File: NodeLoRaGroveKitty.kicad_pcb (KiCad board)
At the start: 2 copper layers, 50 x 50 mm, 42 parts, among them IC1 CP2104, P1 PICKIT PROGRAMMER, P2 Battery, P3 USB_B, P4 A0, P5 D9, P6 I2C, Q1 MMBT2222A, Q2 MMBT2222A, SW1 SW_RESET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

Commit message: PCB 1.0v
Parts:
- removed P1: PICKIT PROGRAMMER, Pin_Headers:Pin_Header_Straight_1x05_Pitch2.54mm
- added G***: LOGO, modules:electronic_cats_logo_4x3, F.Cu at (145.1, 105.9)
- P2: footprint Pin_Headers:Pin_Header_Angled_1x02_Pitch2.54mm -> modules:panelmate_smd_2
- moved C6 51.0 mm to (164.9, 95.4), turned to 270 degrees
- moved R6 50.9 mm to (165.4, 110.0), turned to 0 degrees
- moved Q2 48.8 mm to (164.8, 106.9), turned to 270 degrees
- moved R7 43.8 mm to (160.1, 110.1), turned to 180 degrees
- moved Q1 43.6 mm to (161.0, 106.9), turned to 270 degrees
- moved R10 41.4 mm to (162.4, 95.3), turned to 270 degrees
- moved P2 39.8 mm to (141.9, 124.0), turned to 90 degrees
- moved R14 38.4 mm to (131.2, 96.0)
- moved U1 38.4 mm to (152.4, 125.8)
- moved A1 38.4 mm to (121.7, 87.8)
- moved D1 38.4 mm to (164.7, 128.5)
- moved D2 38.4 mm to (162.0, 128.5)
- moved P4 38.4 mm to (145.2, 127.3)
- moved R13 38.4 mm to (167.2, 95.4)
- moved R15 38.4 mm to (131.2, 98.4)
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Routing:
- net +3V3: track 24.2 -> 226.9 mm, vias 0 -> 10
- net VCC: track 2.89 -> 91.3 mm, vias 0 -> 4
- net GND: track 27.8 -> 102.4 mm, vias 0 -> 14
- net /GPIO13: track 0.00 -> 66.5 mm, vias 0 -> 4
- net /SCL: track 0.00 -> 57.0 mm, vias 0 -> 2
- net /SDA: track 0.00 -> 55.1 mm, vias 0 -> 2
- net /RESET: track 0.00 -> 54.2 mm, vias 0 -> 2
- net /GPIO2: track 35.9 -> 89.2 mm, vias 0 -> 2
- net /A0: track 0.00 -> 52.2 mm, vias 0 -> 2
- net Net-(D4-Pad2): track 0.07 -> 37.9 mm, vias 0 -> 3
- net Net-(D5-Pad1): track 0.00 -> 31.6 mm, vias 0 -> 2
- net Net-(D3-Pad1): track 0.00 -> 29.3 mm, vias 0 -> 1
- net /GPIO0: track 0.00 -> 25.3 mm
- net /SRX: track 0.00 -> 21.3 mm, vias 0 -> 1
- net /STX: track 0.00 -> 20.3 mm, vias 0 -> 1
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- added copper zone on B.Cu, net GND
- added copper zone on F.Cu, net GND
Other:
- board text added: "VCC"
- board text removed: "Vcc"

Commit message: Update Labels
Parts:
- renumbered SW1 to RST
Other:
- board text added: "D13"
- board text added: "D2"
- board text removed: "02"
- board text removed: "13"
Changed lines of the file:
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@@
 (kicad_pcb (version 4) (host pcbnew 4.0.5)
   (general
-    (links 0)
-    (no_connects 1)
+    (links 105)
+    (no_connects 0)
     (area 120.109999 82.589999 170.210001 132.690001)
     (thickness 1.6)
@@
     (tags "LED led 0805 SMD smd SMT smt smdled SMDLED smtled SMTLED")
     (attr smd)
-    (fp_text reference D3 (at 2.8 0 180) (layer F.SilkS)
-      (effects (font (size 1 1) (thickness 0.15)))
-    )
-    (fp_text value CHG (at 5.05 0.05 90) (layer F.SilkS)
+    (fp_text reference D3 (at 2.8 0 180) (layer F.Fab)
+      (effects (font (size 1 1) (thickness 0.15)))
+    )
+    (fp_text value CHG (at 3.64 0.04 90) (layer F.SilkS)
       (effects (font (size 1 1) (thickness 0.15)))
     )
@@
     (tags "LED led 0805 SMD smd SMT smt smdled SMDLED smtled SMTLED")
     (attr smd)
-    (fp_text reference D4 (at -2.7 0.1 360) (layer F.SilkS)
-      (effects (font (size 1 1) (thickness 0.15)))
-    )
-    (fp_text value DONE (at -5.5 -0.05 270) (layer F.SilkS)
+    (fp_text reference D4 (at -2.7 0.1 360) (layer F.Fab)
+      (effects (font (size 1 1) (thickness 0.15)))
+    )
+    (fp_text value DONE (at -4.04 -0.04 270) (layer F.SilkS)
       (effects (font (size 1 1) (thickness 0.15)))
     )
@@
       (effects (font (size 1 1) (thickness 0.15)))
     )
-    (fp_text value Led (at -4.8 0 270) (layer F.SilkS)
+    (fp_text value Led (at -4.8 0 270) (layer F.Fab)
       (effects (font (size 1 1) (thickness 0.15)))
     )
@@
     (tags "Tactile Switch")
     (attr smd)
-    (fp_text reference SW1 (at 0.033329 2.25 90) (layer F.SilkS)
+    (fp_text reference RST (at 0.033329 2.25 90) (layer F.SilkS)
       (effects (font (size 1 1) (thickness 0.15)))
     )
@@
       (xy 1.463092 -2.5146) (xy 1.492024 -2.514153)) (layer F.SilkS) (width 0.01))
   )
-  (gr_text 13 (at 164.41 120.89 90) (layer F.SilkS)
+  (gr_text D13 (at 164.41 120.89 90) (layer F.SilkS)
     (effects (font (size 1.5 1.5) (thickness 0.2)) (justify mirror))
   )
-  (gr_text "02\n" (at 162.41 120.64 90) (layer F.SilkS)
+  (gr_text "D2\n" (at 162.41 120.64 90) (layer F.SilkS)
     (effects (font (size 1.5 1.5) (thickness 0.2)) (justify mirror))
   )

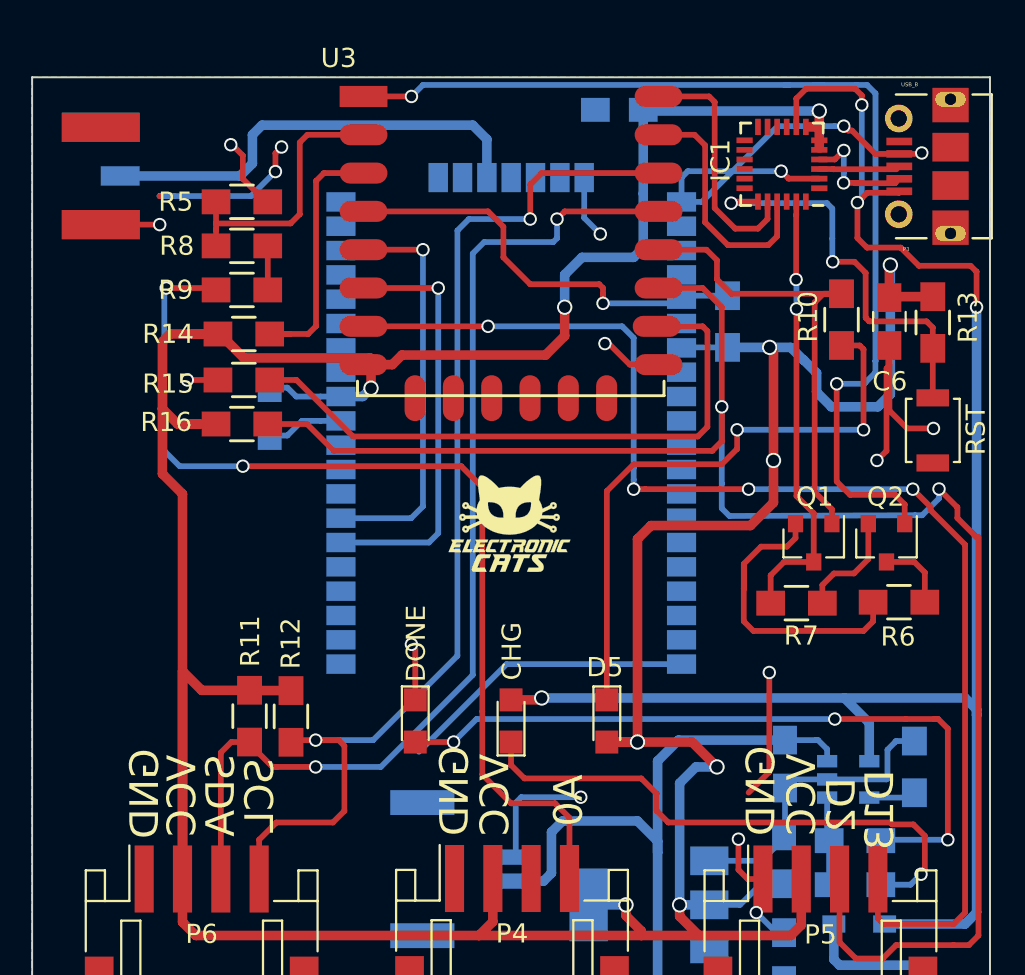
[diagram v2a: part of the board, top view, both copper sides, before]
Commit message: Update inverter label
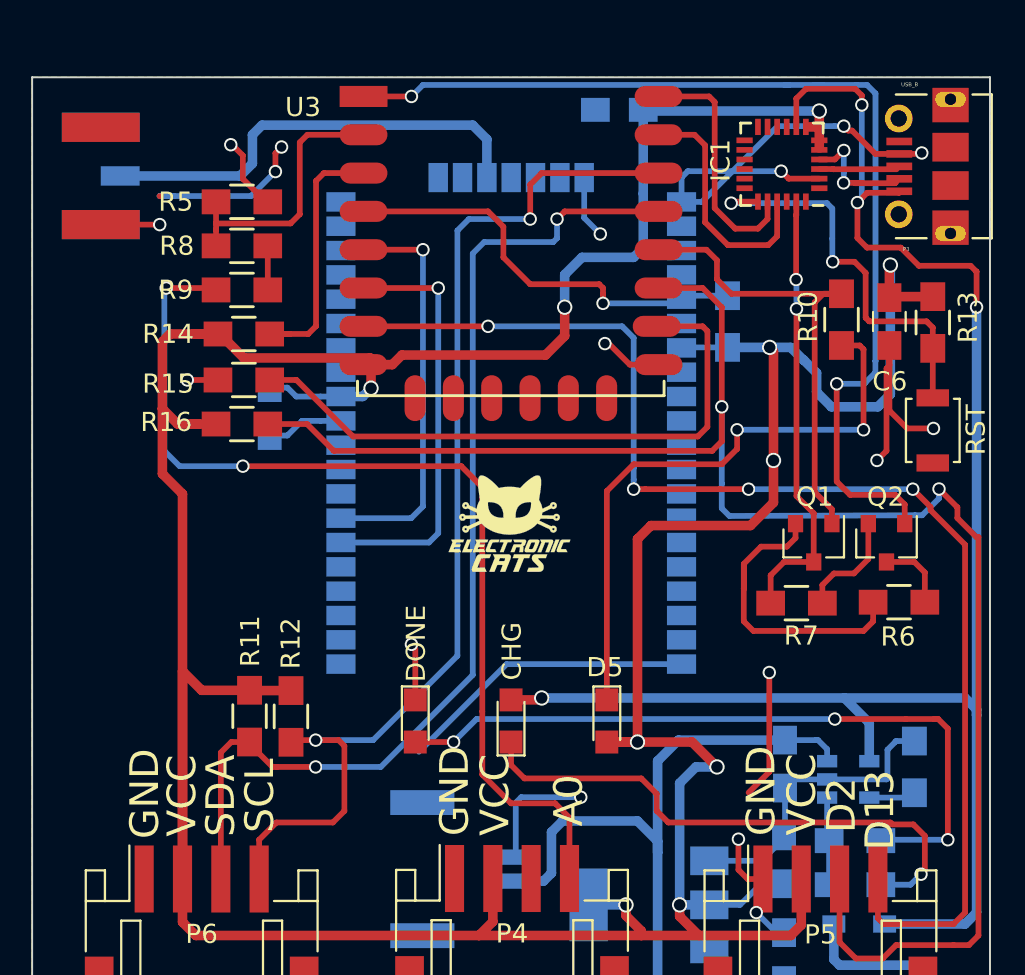
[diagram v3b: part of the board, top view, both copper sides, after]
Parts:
- renumbered MODULE1 to RN2xx3
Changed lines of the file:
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@@
     (descr "Module, ESP-8266, ESP-12, 16 pad, SMD")
     (tags "Module ESP-8266 ESP8266")
-    (fp_text reference U3 (at -2 -2) (layer F.SilkS)
+    (fp_text reference U3 (at -3.86 0.56) (layer F.SilkS)
       (effects (font (size 1 1) (thickness 0.15)))
     )
@@
   (module Library:RN2483 (layer B.Cu)
     (at 154.05858 114.544404 180)
-    (fp_text reference MODULE1 (at 2.8956 1.4478 180) (layer B.SilkS)
+    (fp_text reference RN2xx3 (at 2.95858 -1.255596 180) (layer B.SilkS)
       (effects (font (size 1 1) (thickness 0.15)) (justify mirror))
     )
@@
   )
   (gr_text D13 (at 164.41 120.89 90) (layer F.SilkS)
-    (effects (font (size 1.5 1.5) (thickness 0.2)) (justify mirror))
+    (effects (font (size 1.5 1.5) (thickness 0.2)))
   )
   (gr_text "D2\n" (at 162.41 120.64 90) (layer F.SilkS)
-    (effects (font (size 1.5 1.5) (thickness 0.2)) (justify mirror))
+    (effects (font (size 1.5 1.5) (thickness 0.2)))
   )
   (gr_text A0 (at 148.16 120.39 90) (layer F.SilkS)
-    (effects (font (size 1.5 1.5) (thickness 0.2)) (justify mirror))
+    (effects (font (size 1.5 1.5) (thickness 0.2)))
   )
   (gr_text "SCL\n" (at 132.04 120.14 90) (layer F.SilkS)
-    (effects (font (size 1.5 1.5) (thickness 0.2)) (justify mirror))
+    (effects (font (size 1.5 1.5) (thickness 0.2)))
   )
   (gr_text "SDA\n" (at 130 120.14 90) (layer F.SilkS)
-    (effects (font (size 1.5 1.5) (thickness 0.2)) (justify mirror))
+    (effects (font (size 1.5 1.5) (thickness 0.2)))
   )
   (gr_text VCC (at 127.98 120.14 90) (layer F.SilkS)
-    (effects (font (size 1.5 1.5) (thickness 0.2)) (justify mirror))
+    (effects (font (size 1.5 1.5) (thickness 0.2)))
   )
   (gr_text VCC (at 144.32 120.1 90) (layer F.SilkS)
-    (effects (font (size 1.5 1.5) (thickness 0.2)) (justify mirror))
+    (effects (font (size 1.5 1.5) (thickness 0.2)))
   )
   (gr_text "VCC\n\n" (at 161.54 120.08 90) (layer F.SilkS)
-    (effects (font (size 1.5 1.5) (thickness 0.2)) (justify mirror))
+    (effects (font (size 1.5 1.5) (thickness 0.2)))
   )
   (gr_text GND (at 158.21 119.89 90) (layer F.SilkS)
-    (effects (font (size 1.5 1.5) (thickness 0.2)) (justify mirror))
+    (effects (font (size 1.5 1.5) (thickness 0.2)))
   )
   (gr_text GND (at 142.21 119.89 90) (layer F.SilkS)
-    (effects (font (size 1.5 1.5) (thickness 0.2)) (justify mirror))
+    (effects (font (size 1.5 1.5) (thickness 0.2)))
   )
   (gr_text GND (at 126.035 120.04 90) (layer F.SilkS)
-    (effects (font (size 1.5 1.5) (thickness 0.2)) (justify mirror))
+    (effects (font (size 1.5 1.5) (thickness 0.2)))
   )
   (gr_line (start 170.16 82.64) (end 170.16 132.64) (layer Edge.Cuts) (width 0.1))

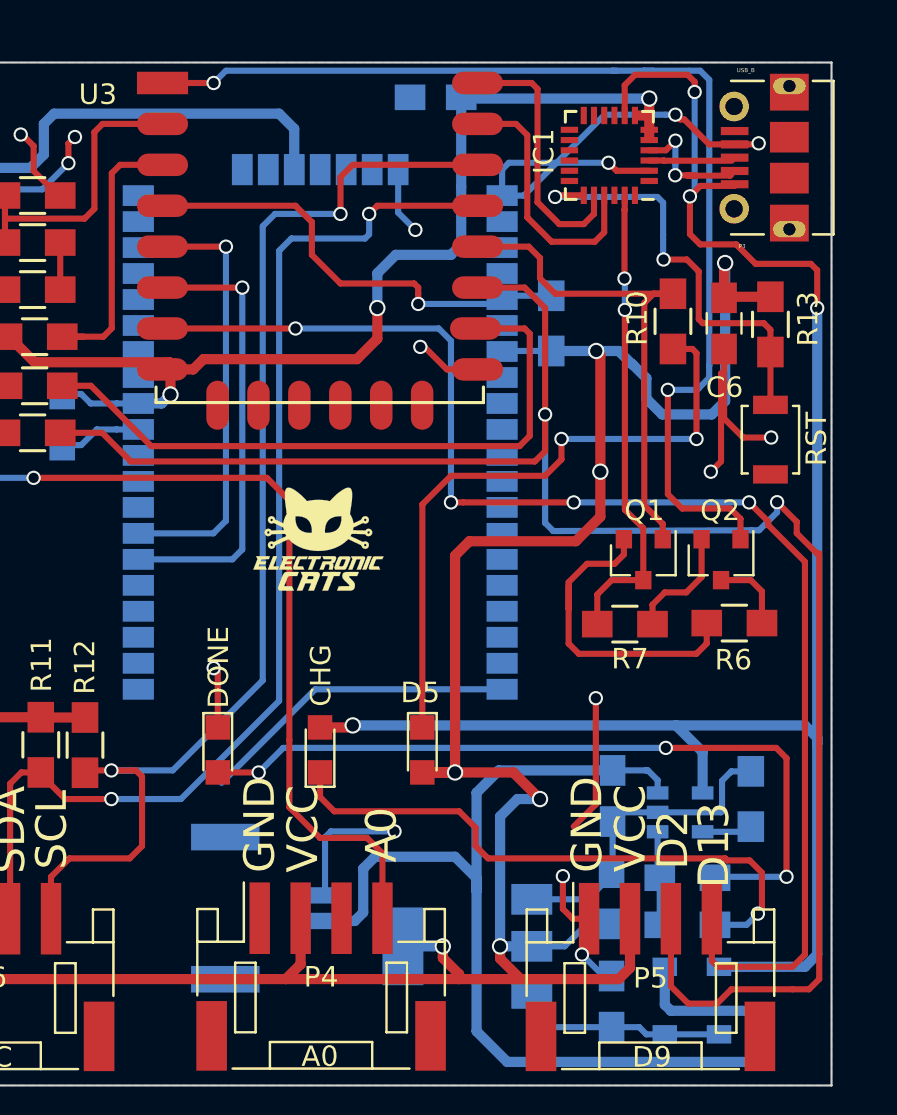
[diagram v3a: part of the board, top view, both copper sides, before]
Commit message: Change USB with libraries
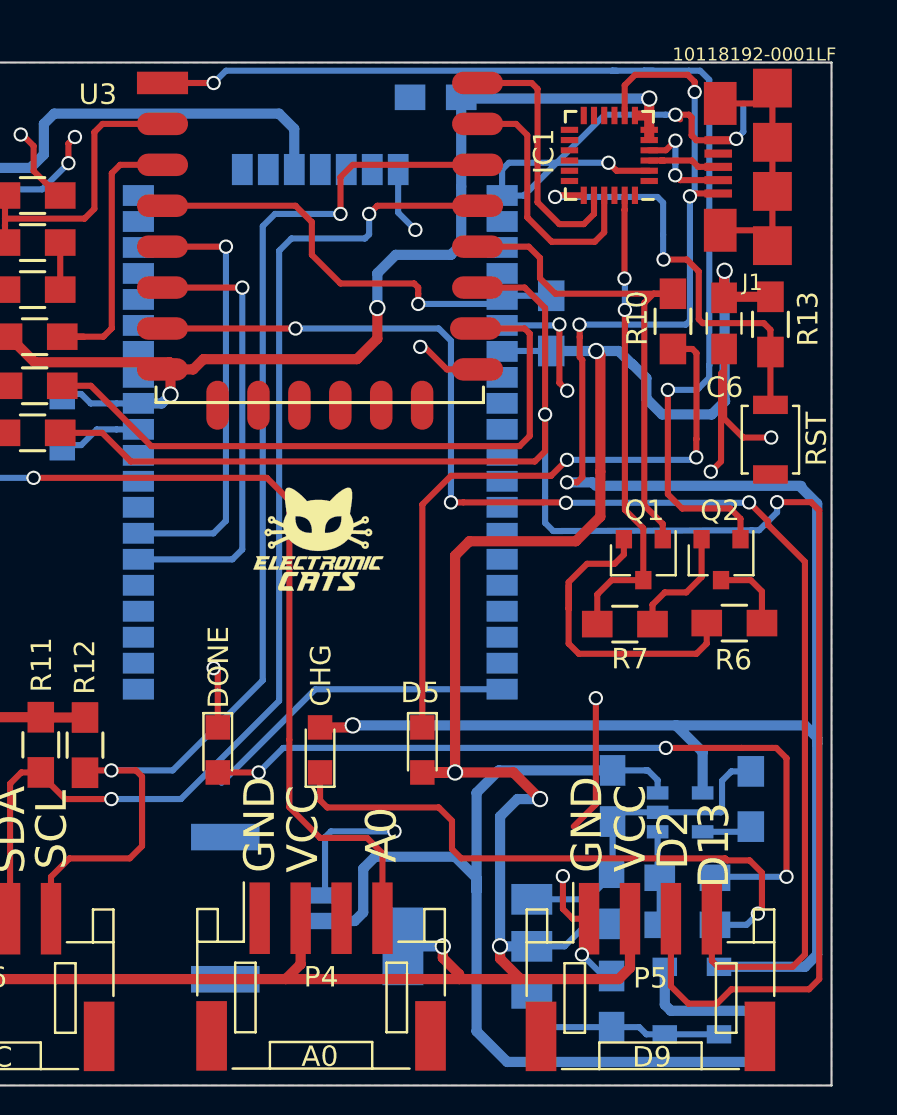
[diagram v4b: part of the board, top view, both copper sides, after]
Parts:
- removed P3: USB_B, LoraCat:MOLEX_105017-0001
- removed RN2xx3: RN2903, Library:RN2483
- added J1: 10118192-0001LF, 10118192-0001LF:10118192-0001LF, F.Cu at (168.7, 87.7)
- added MODULE1: RN2903, Library:RN2483, B.Cu at (154.1, 114.5)
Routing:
- net Net-(J1-PadM1): track 0.00 -> 13.4 mm
- net VCC: track 91.3 -> 102.6 mm, vias 4 -> 5
- net GND: track 102.4 -> 110.1 mm, vias 14 -> 16
- net Net-(IC1-Pad4): track 6.37 -> 5.37 mm
- net /GPIO2: track 89.2 -> 90.1 mm
- net +3V3: track 226.9 -> 226.2 mm, vias 10 -> 9

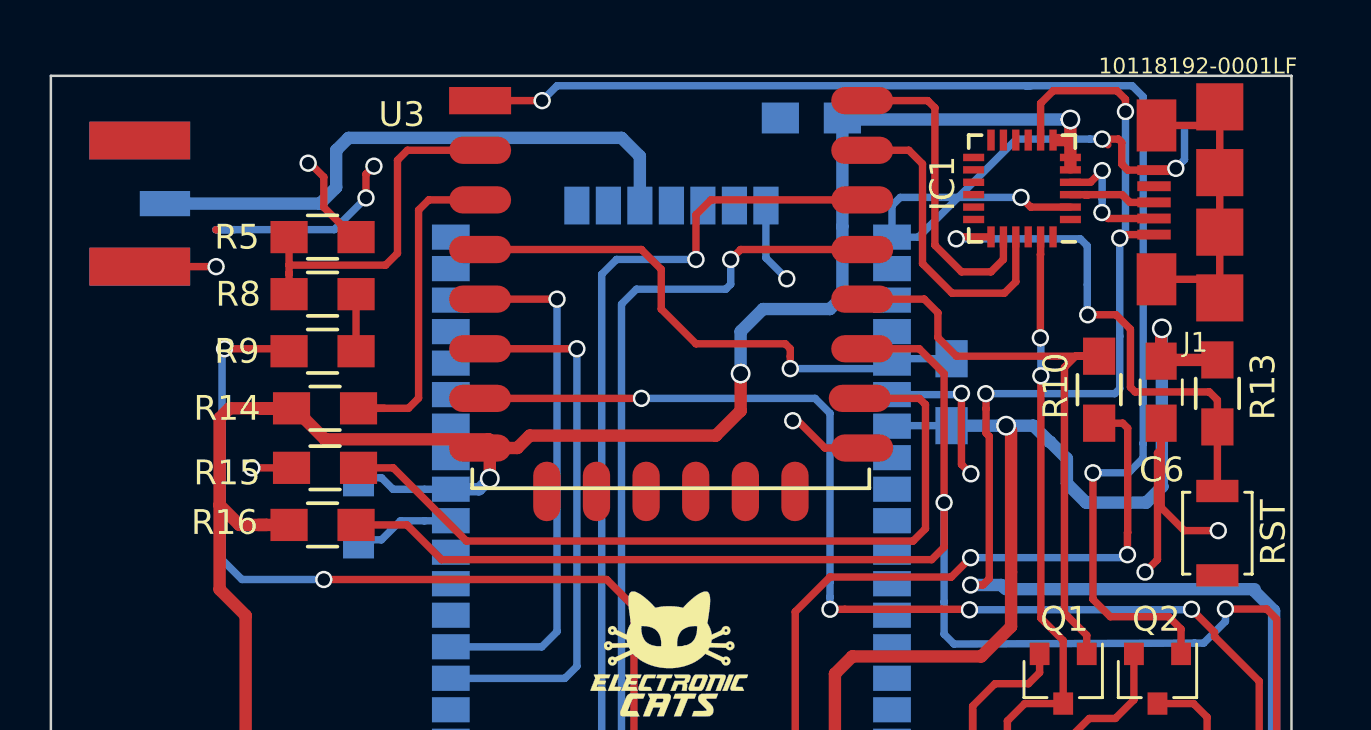
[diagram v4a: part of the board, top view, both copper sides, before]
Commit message: Add new RN and fix ways
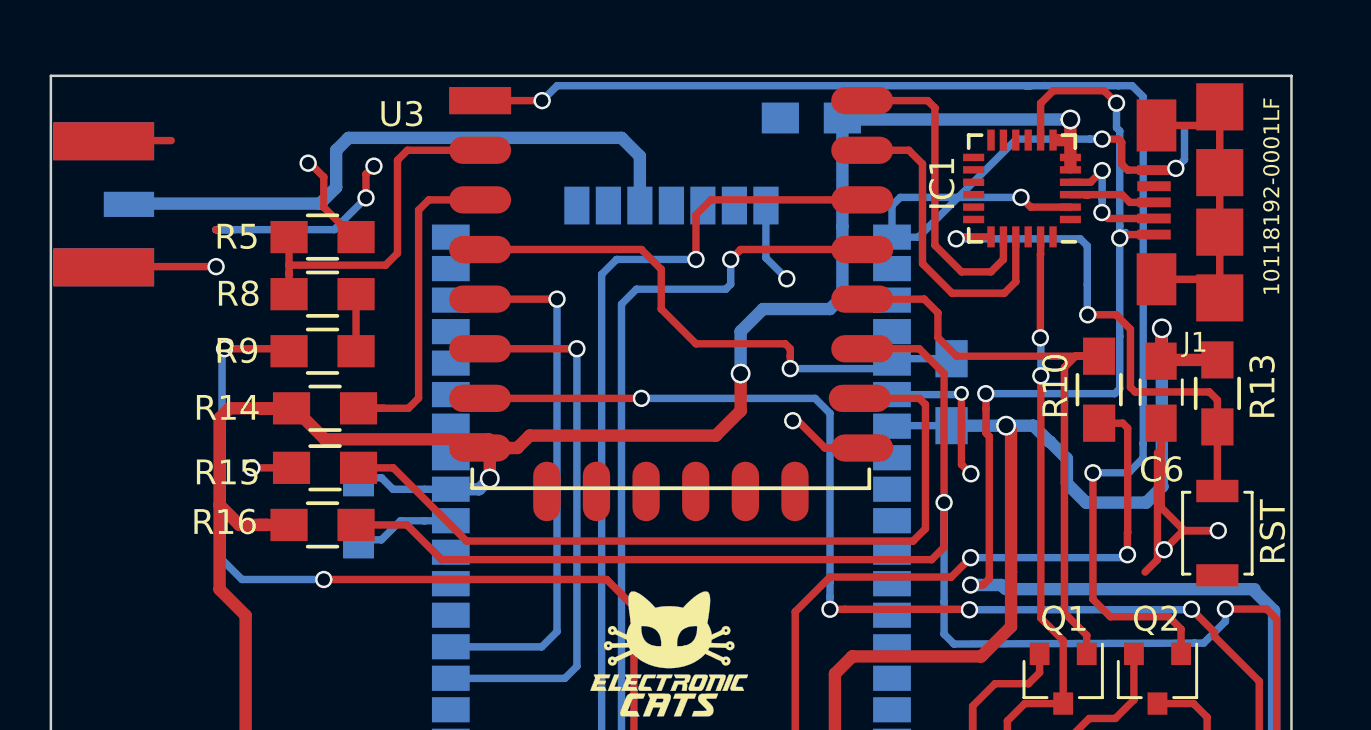
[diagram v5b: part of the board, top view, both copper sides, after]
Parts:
- moved A1 1.45 mm to (120.3, 87.8)
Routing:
- net GND: track 110.1 -> 112.3 mm
- net Net-(A1-Pad1): track 23.4 -> 24.9 mm
